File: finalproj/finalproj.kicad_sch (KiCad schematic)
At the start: 35 parts, among them J5 Stepper_Motor_Controller, J7 LIDAR_Connector, J9 RPI_UART_Conn, U2 LM1085-12, U3 LM1085-5.0, U4 LM1085-3.3, U5 L298N

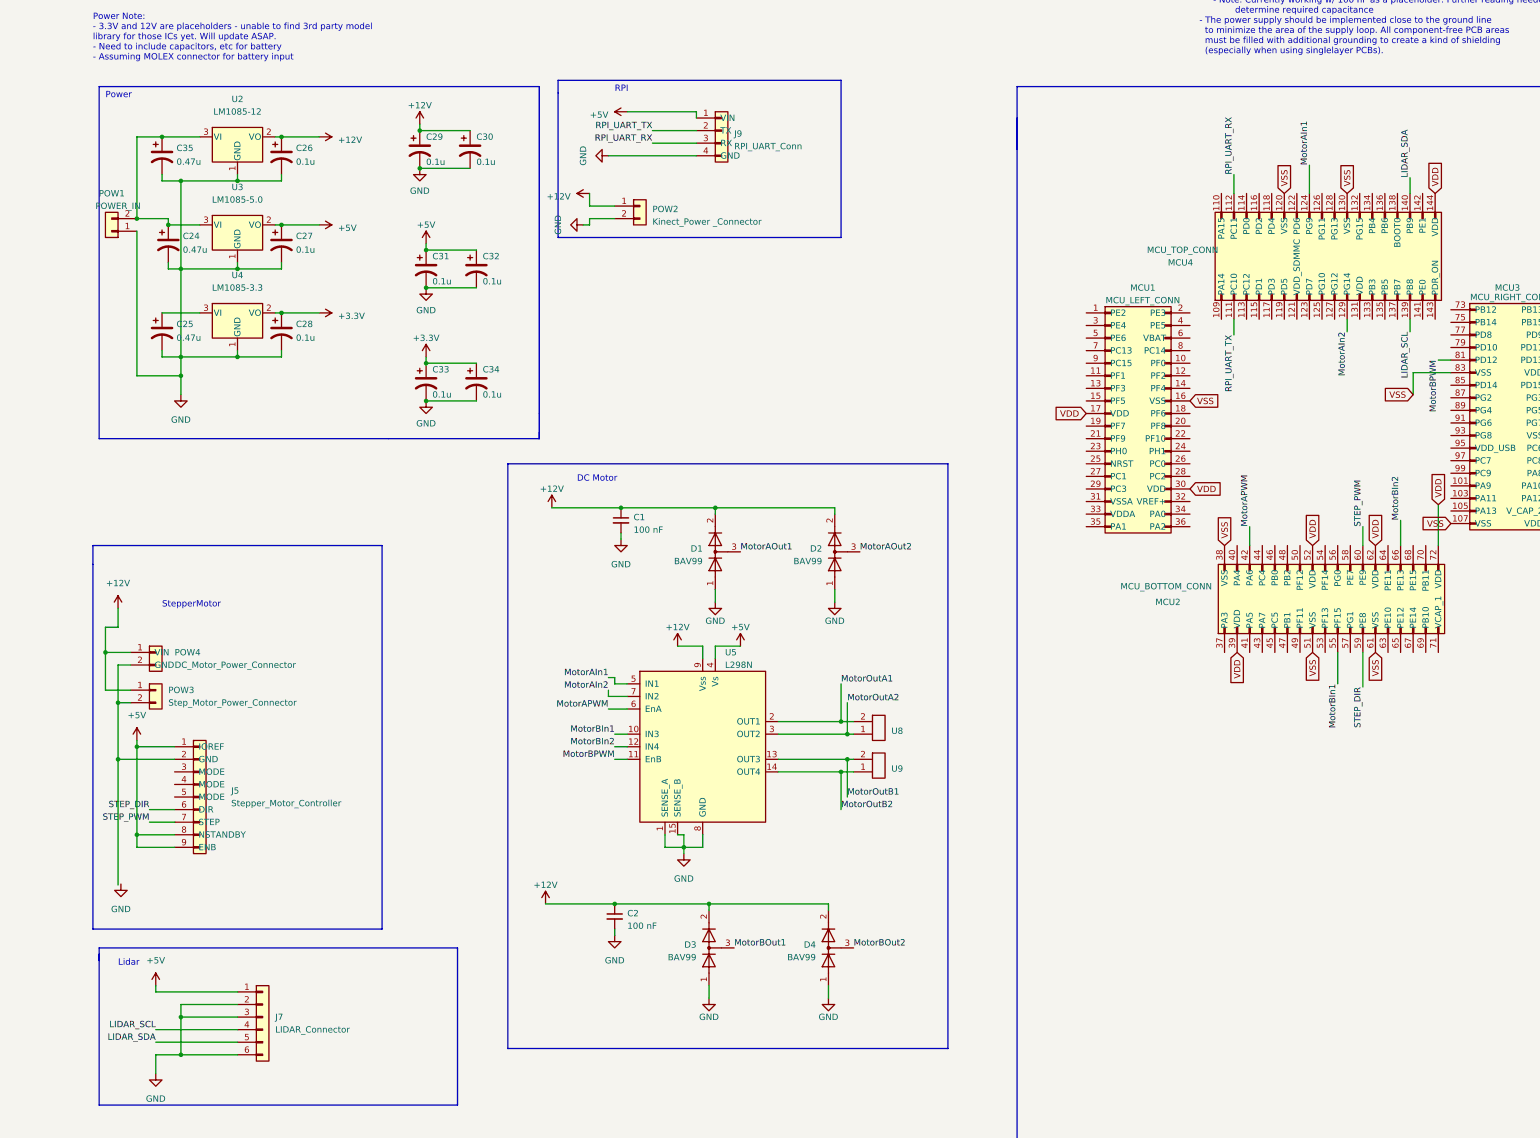
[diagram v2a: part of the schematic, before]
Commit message: finished schematic with sockets\n initial pcb
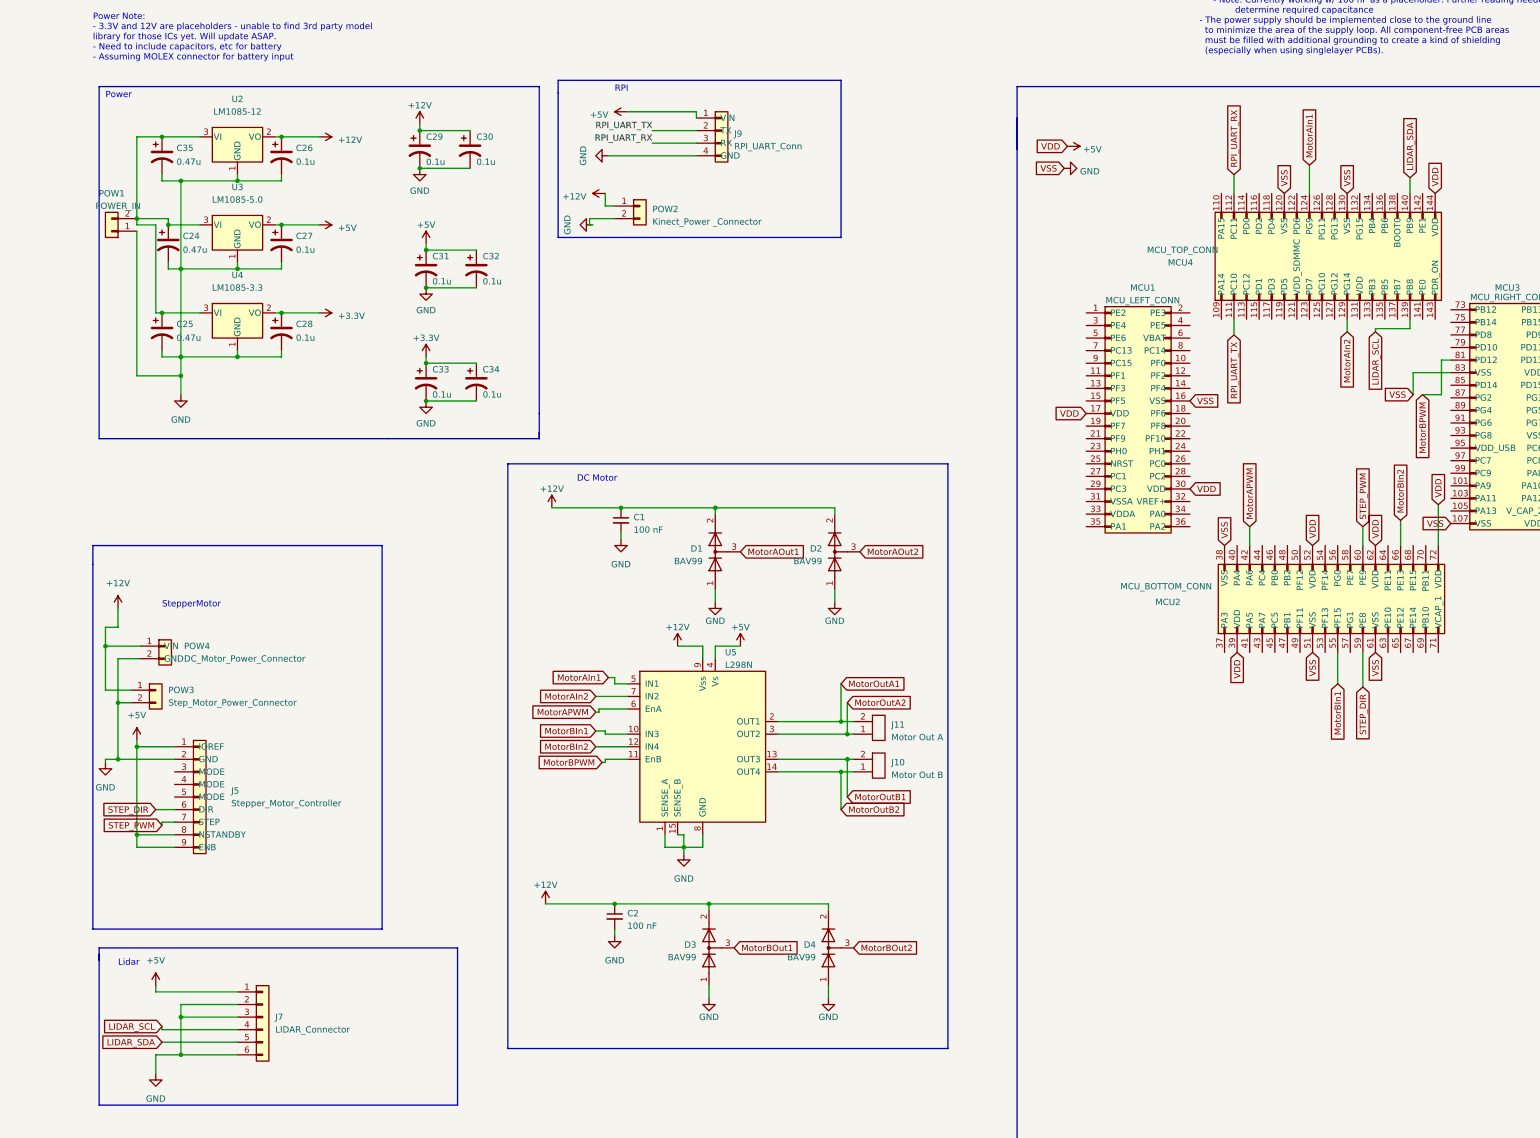
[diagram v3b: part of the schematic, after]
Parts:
- removed U8, U9: ~, symbol finalproj:Motor_Output_Connector
- added J10: Motor Out B, TerminalBlock_Phoenix:TerminalBlock_Phoenix_PT-1,5-2-5.0-H_1x02_P5.00mm_Horizontal, symbol finalProj:Motor_Output_Connector
- added J11: Motor Out A, TerminalBlock_Phoenix:TerminalBlock_Phoenix_PT-1,5-2-5.0-H_1x02_P5.00mm_Horizontal, symbol finalProj:Motor_Output_Connector
- C1, C2: footprint (none) -> Capacitor_SMD:C_0805_2012Metric
- J7: footprint (none) -> Connector_Phoenix_MC:PhoenixContact_MCV_1,5_6-G-3.81_1x06_P3.81mm_Vertical
- J9: footprint (none) -> Connector_Phoenix_MC:PhoenixContact_MCV_1,5_4-G-3.81_1x04_P3.81mm_Vertical
- POW1: footprint (none) -> XT60_YELLOW:AMASS_XT60PB-M
- POW2: footprint (none) -> TerminalBlock_Phoenix:TerminalBlock_Phoenix_PT-1,5-2-5.0-H_1x02_P5.00mm_Horizontal
- U2, U3, U4: footprint (none) -> LM1085IT-5.0:TO254P1054X470X1955-3
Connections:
- net VDD is gone; now on net +5V: MCU1.17 (VDD), MCU1.30 (VDD), MCU2.39 (VDD), MCU2.52 (VDD), MCU2.62 (VDD), MCU2.72 (VDD), MCU3.108 (VDD), MCU3.84 (VDD), MCU4.144 (VDD)
- net VSS is gone; now on net GND: MCU1.16 (VSS), MCU2.38 (VSS), MCU2.51 (VSS), MCU2.61 (VSS), MCU3.107 (VSS), MCU3.83 (VSS), MCU4.120 (VSS), MCU4.130 (VSS)
- net GND: now also J5.2 (GND), POW3.2 (GND), POW4.2 (GND)
- net MotorOutA1: now also J11.2 (Out-)
- net MotorOutA2: now also J11.1 (Out+)
- net MotorOutB1: now also J10.2 (Out-)
- net MotorOutB2: now also J10.1 (Out+)
- net at C24.1, C35.1, POW1.2 (Pin_2)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: now also C25.1, U4.3 (VI)
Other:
- moved on the sheet: POW4

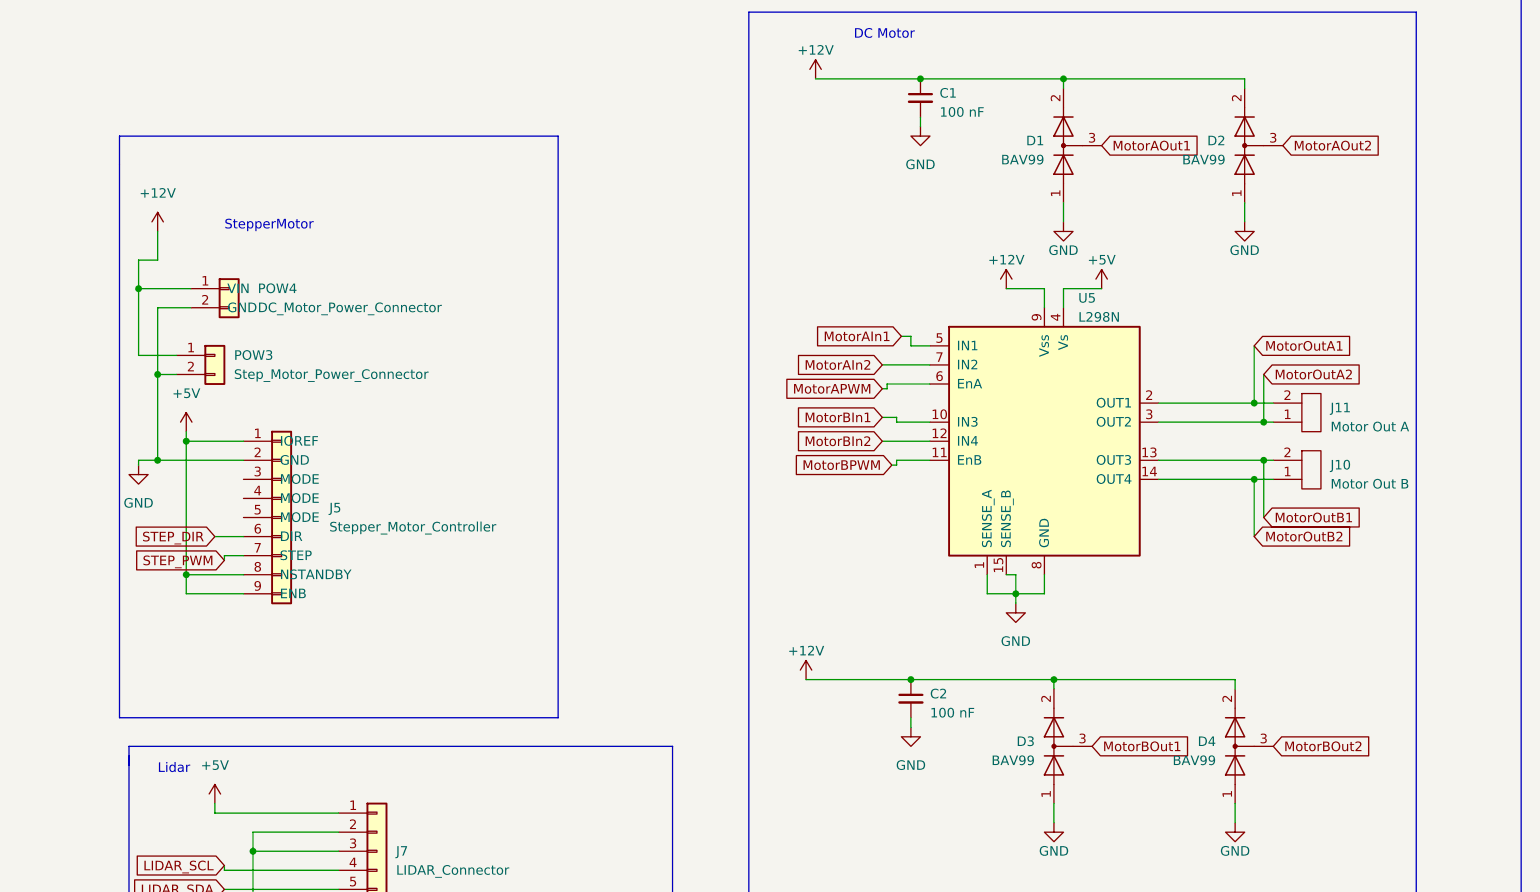
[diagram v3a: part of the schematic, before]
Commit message: pcb edits fixed pcb errors
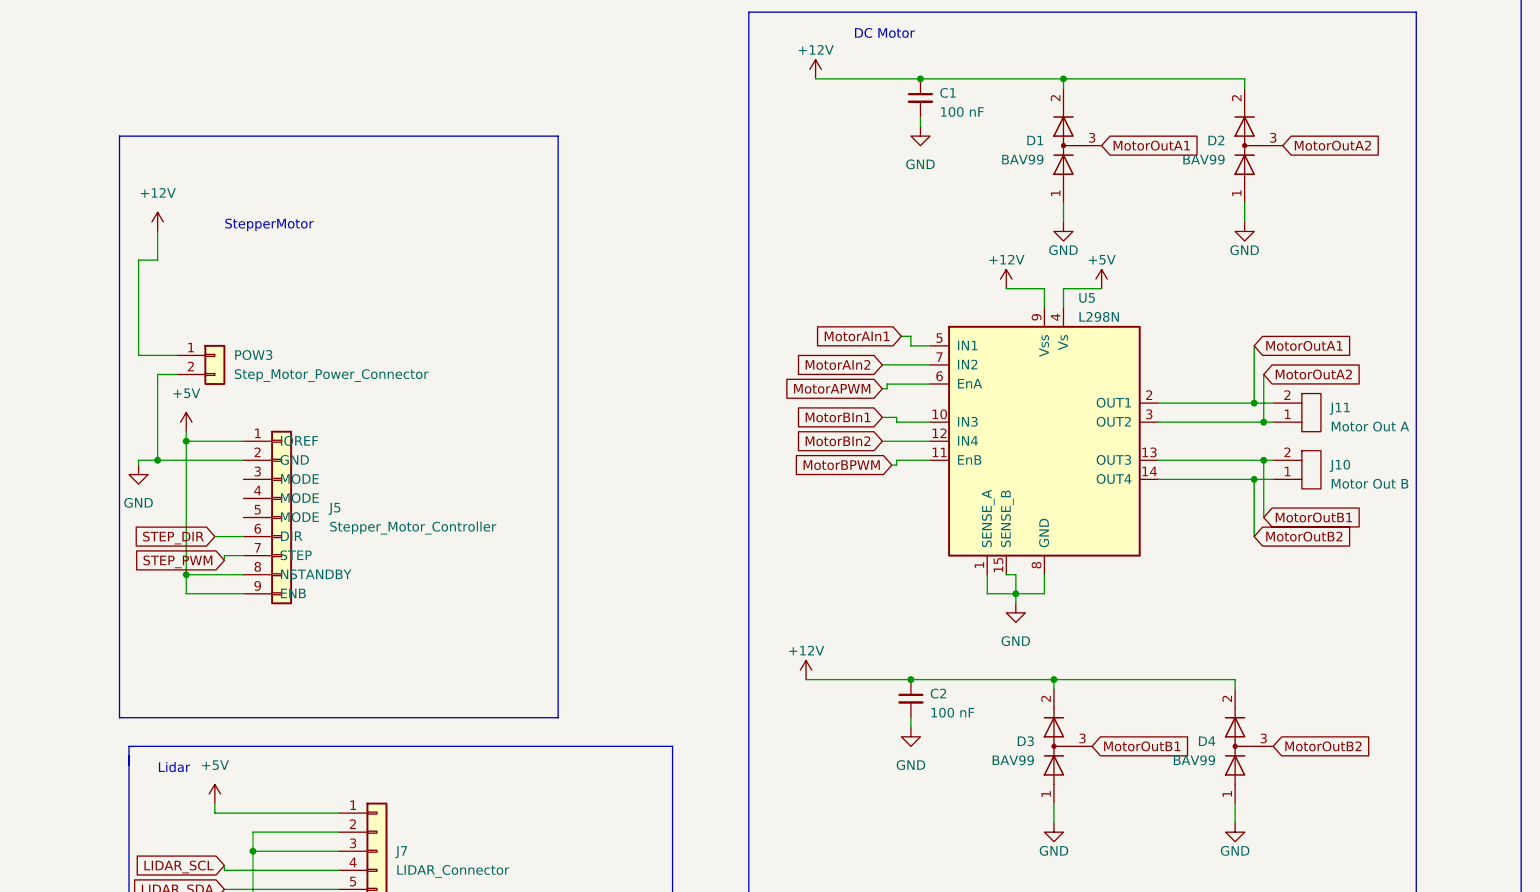
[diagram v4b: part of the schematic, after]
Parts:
- removed POW4: DC_Motor_Power_Connector, TerminalBlock_Phoenix:TerminalBlock_Phoenix_PT-1,5-2-3.5-H_1x02_P3.50mm_Horizontal, symbol finalProj:Motor_Power_Connector
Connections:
- net MotorAOut1 is gone; now on net MotorOutA1: D1.3 (K)
- net MotorAOut2 is gone; now on net MotorOutA2: D2.3 (K)
- net MotorBOut1 is gone; now on net MotorOutB1: D3.3 (K)
- net MotorBOut2 is gone; now on net MotorOutB2: D4.3 (K)
